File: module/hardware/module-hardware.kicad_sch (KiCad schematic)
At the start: 48 parts

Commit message: Start work on dsub pinout/connections
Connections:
- net +5V: now also J?.1 (Pin_1)
- net ASUM: now also J?.9 (Pin_9)
- net GND: now also J?.10 (Pin_10), J?.8 (Pin_8)
- net GPIO16_EXTRA: now reaches U?.27 (GPIO16)
- net GPIO17_DRDY: now reaches U?.28 (GPIO17)
- net GPIO18_SCK: now reaches U?.29 (GPIO18)
- net GPIO19_SDIN: now reaches U?.30 (GPIO19)
- net GPIO20_SDOUT: now reaches U?.31 (GPIO20)
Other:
- moved on the sheet: J?
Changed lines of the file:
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@@
   (junction (at 88.9 54.61) (diameter 0) (color 0 0 0 0)
+  )
+  (junction (at 76.2 191.77) (diameter 0) (color 0 0 0 0)
   )
   (junction (at 303.53 85.09) (diameter 0) (color 0 0 0 0)
@@
     (stroke (width 0) (type default) (color 0 0 0 0))
   )
-  (wire (pts (xy 240.03 237.49) (xy 243.84 237.49))
+  (wire (pts (xy 58.42 181.61) (xy 60.96 181.61))
+    (stroke (width 0) (type default) (color 0 0 0 0))
+  )
+  (wire (pts (xy 240.03 237.49) (xy 257.81 237.49))
     (stroke (width 0) (type default) (color 0 0 0 0))
   )
@@
     (stroke (width 0) (type default) (color 0 0 0 0))
   )
+  (wire (pts (xy 76.2 189.23) (xy 76.2 191.77))
+    (stroke (width 0) (type default) (color 0 0 0 0))
+  )
   (wire (pts (xy 180.34 123.19) (xy 180.34 130.81))
     (stroke (width 0) (type default) (color 0 0 0 0))
@@
     (stroke (width 0) (type default) (color 0 0 0 0))
   )
+  (wire (pts (xy 241.3 97.79) (xy 261.62 97.79))
+    (stroke (width 0) (type default) (color 0 0 0 0))
+  )
   (wire (pts (xy 179.07 34.29) (xy 179.07 30.48))
     (stroke (width 0) (type default) (color 0 0 0 0))
@@
     (stroke (width 0) (type default) (color 0 0 0 0))
   )
+  (wire (pts (xy 73.66 191.77) (xy 76.2 191.77))
+    (stroke (width 0) (type default) (color 0 0 0 0))
+  )
   (wire (pts (xy 57.15 54.61) (xy 63.5 54.61))
     (stroke (width 0) (type default) (color 0 0 0 0))
@@
     (stroke (width 0) (type default) (color 0 0 0 0))
   )
+  (wire (pts (xy 73.66 189.23) (xy 76.2 189.23))
+    (stroke (width 0) (type default) (color 0 0 0 0))
+  )
   (wire (pts (xy 60.96 240.03) (xy 71.12 240.03))
     (stroke (width 0) (type default) (color 0 0 0 0))
@@
     (stroke (width 0) (type default) (color 0 0 0 0))
   )
+  (wire (pts (xy 76.2 194.31) (xy 76.2 191.77))
+    (stroke (width 0) (type default) (color 0 0 0 0))
+  )
   (wire (pts (xy 289.56 30.48) (xy 289.56 34.29))
     (stroke (width 0) (type default) (color 0 0 0 0))
@@
     (stroke (width 0) (type default) (color 0 0 0 0))
   )
+  (wire (pts (xy 241.3 102.87) (xy 261.62 102.87))
+    (stroke (width 0) (type default) (color 0 0 0 0))
+  )
   (wire (pts (xy 201.93 30.48) (xy 201.93 34.29))
     (stroke (width 0) (type default) (color 0 0 0 0))
@@
     (stroke (width 0) (type default) (color 0 0 0 0))
   )
+  (wire (pts (xy 241.3 107.95) (xy 261.62 107.95))
+    (stroke (width 0) (type default) (color 0 0 0 0))
+  )
   (wire (pts (xy 80.01 130.81) (xy 74.93 130.81))
     (stroke (width 0) (type default) (color 0 0 0 0))
@@
     (stroke (width 0) (type default) (color 0 0 0 0))
   )
+  (wire (pts (xy 58.42 179.07) (xy 58.42 181.61))
+    (stroke (width 0) (type default) (color 0 0 0 0))
+  )
   (wire (pts (xy 339.09 101.6) (xy 351.79 101.6))
     (stroke (width 0) (type default) (color 0 0 0 0))
@@
     (stroke (width 0) (type default) (color 0 0 0 0))
   )
+  (wire (pts (xy 241.3 100.33) (xy 261.62 100.33))
+    (stroke (width 0) (type default) (color 0 0 0 0))
+  )
   (wire (pts (xy 162.56 111.76) (xy 162.56 113.03))
     (stroke (width 0) (type default) (color 0 0 0 0))
   )
+  (wire (pts (xy 52.07 191.77) (xy 60.96 191.77))
+    (stroke (width 0) (type default) (color 0 0 0 0))
+  )
   (wire (pts (xy 255.27 41.91) (xy 255.27 44.45))
     (stroke (width 0) (type default) (color 0 0 0 0))
@@
   )
   (wire (pts (xy 314.96 85.09) (xy 303.53 85.09))
+    (stroke (width 0) (type default) (color 0 0 0 0))
+  )
+  (wire (pts (xy 241.3 105.41) (xy 261.62 105.41))
     (stroke (width 0) (type default) (color 0 0 0 0))
   )
@@
     (effects (font (size 1.27 1.27)) (justify right bottom))
   )
+  (label "GPIO18_SCK" (at 261.62 102.87 180)
+    (effects (font (size 1.27 1.27)) (justify right bottom))
+  )
   (label "GPIO28_ADC2" (at 336.55 104.14 0)
     (effects (font (size 1.27 1.27)) (justify left bottom))
   )
+  (label "ASUM" (at 52.07 191.77 0)
+    (effects (font (size 1.27 1.27)) (justify left bottom))
+  )
   (label "GPIO26_ADC0" (at 336.55 80.01 0)
     (effects (font (size 1.27 1.27)) (justify left bottom))
+  )
+  (label "GPIO17_DRDY" (at 261.62 100.33 180)
+    (effects (font (size 1.27 1.27)) (justify right bottom))
+  )
+  (label "ASUM" (at 257.81 237.49 180)
+    (effects (font (size 1.27 1.27)) (justify right bottom))
   )
   (label "GPIO29_ADC3" (at 367.03 104.14 0)
@@
     (effects (font (size 1.27 1.27)) (justify right bottom))
   )
+  (label "GPIO20_SDOUT" (at 261.62 107.95 180)
+    (effects (font (size 1.27 1.27)) (justify right bottom))
+  )
+  (label "GPIO16_EXTRA" (at 261.62 97.79 180)
+    (effects (font (size 1.27 1.27)) (justify right bottom))
+  )
   (label "GPIO10_DAC_SCK" (at 261.62 82.55 180)
     (effects (font (size 1.27 1.27)) (justify right bottom))
@@
     (effects (font (size 1.27 1.27)) (justify right bottom))
   )
+  (label "GPIO19_SDIN" (at 261.62 105.41 180)
+    (effects (font (size 1.27 1.27)) (justify right bottom))
+  )
   (label "GPIO11_DAC_SDAT" (at 151.13 227.33 0)
     (effects (font (size 1.27 1.27)) (justify left bottom))
@@
   (label "GPIO9_DAC_CSB" (at 151.13 234.95 0)
     (effects (font (size 1.27 1.27)) (justify left bottom))
-  )
-  (global_label "ASUM" (shape output) (at 243.84 237.49 0) (fields_autoplaced)
-    (effects (font (size 1.27 1.27)) (justify left))
-    (property "Intersheet References" "${INTERSHEET_REFS}" (id 0) (at 251.3331 237.4106 0)
-      (effects (font (size 1.27 1.27)) (justify left) hide)
-    )
   )
   (symbol (lib_id "power:PWR_FLAG") (at 92.71 38.1 0) (unit 1)
@@
     (pin "1")
   )
+  (symbol (lib_id "power:+5V") (at 58.42 179.07 0) (unit 1)
+    (in_bom yes) (on_board yes) (fields_autoplaced)
+    (property "Reference" "#PWR?" (id 0) (at 58.42 182.88 0)
+      (effects (font (size 1.27 1.27)) hide)
+    )
+    (property "Value" "+5V" (id 1) (at 58.42 173.99 0))
+    (property "Footprint" "" (id 2) (at 58.42 179.07 0)
+      (effects (font (size 1.27 1.27)) hide)
+    )
+    (property "Datasheet" "" (id 3) (at 58.42 179.07 0)
+      (effects (font (size 1.27 1.27)) hide)
+    )
+    (pin "1")
+  )
   (symbol (lib_id "Device:R") (at 173.99 62.23 90) (unit 1)
     (in_bom yes) (on_board yes)
@@
     (pin "2")
   )
-  (symbol (lib_id "Connector_Generic:Conn_02x05_Odd_Even") (at 66.04 193.04 0) (unit 1)
-    (in_bom yes) (on_board yes) (fields_autoplaced)
-    (property "Reference" "J?" (id 0) (at 67.31 180.975 0))
-    (property "Value" "Conn_02x05_Odd_Even" (id 1) (at 67.31 183.515 0))
-    (property "Footprint" "" (id 2) (at 66.04 193.04 0)
-      (effects (font (size 1.27 1.27)) hide)
-    )
-    (property "Datasheet" "~" (id 3) (at 66.04 193.04 0)
+  (symbol (lib_id "Connector_Generic:Conn_02x05_Odd_Even") (at 66.04 186.69 0) (unit 1)
+    (in_bom yes) (on_board yes)
+    (property "Reference" "J?" (id 0) (at 67.31 174.625 0))
+    (property "Value" "Conn_02x05_Odd_Even" (id 1) (at 72.39 177.8 0))
+    (property "Footprint" "" (id 2) (at 66.04 186.69 0)
+      (effects (font (size 1.27 1.27)) hide)
+    )
+    (property "Datasheet" "~" (id 3) (at 66.04 186.69 0)
       (effects (font (size 1.27 1.27)) hide)
     )
@@
     (pin "1")
   )
-  (symbol (lib_id "Connector_Generic:Conn_02x05_Odd_Even") (at 103.505 192.405 0) (unit 1)
-    (in_bom yes) (on_board yes) (fields_autoplaced)
-    (property "Reference" "J?" (id 0) (at 104.775 180.34 0))
-    (property "Value" "Conn_02x05_Odd_Even" (id 1) (at 104.775 182.88 0))
-    (property "Footprint" "" (id 2) (at 103.505 192.405 0)
-      (effects (font (size 1.27 1.27)) hide)
-    )
-    (property "Datasheet" "~" (id 3) (at 103.505 192.405 0)
+  (symbol (lib_id "Connector_Generic:Conn_02x05_Odd_Even") (at 109.22 186.69 0) (unit 1)
+    (in_bom yes) (on_board yes) (fields_autoplaced)
+    (property "Reference" "J?" (id 0) (at 110.49 174.625 0))
+    (property "Value" "Conn_02x05_Odd_Even" (id 1) (at 110.49 177.165 0))
+    (property "Footprint" "" (id 2) (at 109.22 186.69 0)
+      (effects (font (size 1.27 1.27)) hide)
+    )
+    (property "Datasheet" "~" (id 3) (at 109.22 186.69 0)
       (effects (font (size 1.27 1.27)) hide)
     )
@@
     )
     (property "Datasheet" "" (id 3) (at 187.96 143.51 0)
+      (effects (font (size 1.27 1.27)) hide)
+    )
+    (pin "1")
+  )
+  (symbol (lib_id "power:GND") (at 76.2 194.31 0) (unit 1)
+    (in_bom yes) (on_board yes) (fields_autoplaced)
+    (property "Reference" "#PWR?" (id 0) (at 76.2 200.66 0)
+      (effects (font (size 1.27 1.27)) hide)
+    )
+    (property "Value" "GND" (id 1) (at 76.2 199.39 0))
+    (property "Footprint" "" (id 2) (at 76.2 194.31 0)
+      (effects (font (size 1.27 1.27)) hide)
+    )
+    (property "Datasheet" "" (id 3) (at 76.2 194.31 0)
       (effects (font (size 1.27 1.27)) hide)
     )
@@
       (reference "#PWR?") (unit 1) (value "GND") (footprint "")
     )
+    (path "/1eced8f1-fcc8-4121-ae1f-727d47435957"
+      (reference "#PWR?") (unit 1) (value "+5V") (footprint "")
+    )
     (path "/24f789e3-a318-4855-a56f-29afa0155580"
       (reference "#PWR?") (unit 1) (value "+3V3") (footprint "")
@@
       (reference "#PWR?") (unit 1) (value "GND") (footprint "")
     )
+    (path "/b2a71297-139f-414d-9936-936167d27c2a"
+      (reference "#PWR?") (unit 1) (value "GND") (footprint "")
+    )

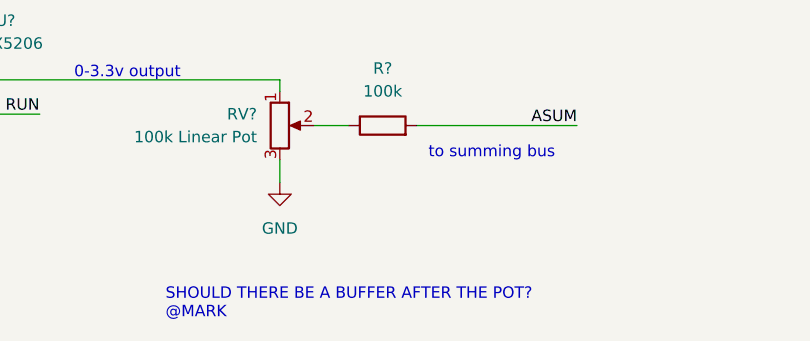
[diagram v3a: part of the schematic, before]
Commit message: Add module schematic TODO
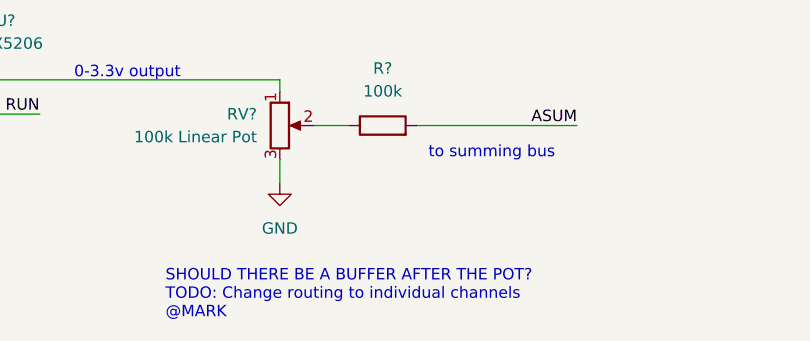
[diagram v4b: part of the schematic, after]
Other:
- note added: "SHOULD THERE BE A BUFFER AFTER THE POT? TODO: Change routing to individual channels @MARK"
- note removed: "SHOULD THERE BE A BUFFER AFTER THE POT? @MARK"
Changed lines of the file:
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@@
     (effects (font (size 2.54 2.54) (thickness 0.508) bold italic) (justify left bottom))
   )
-  (text "SHOULD THERE BE A BUFFER AFTER THE POT?\n@MARK" (at 212.09 259.08 0)
+  (text "SHOULD THERE BE A BUFFER AFTER THE POT?\nTODO: Change routing to individual channels\n@MARK"
+    (at 212.09 259.08 0)
     (effects (font (size 1.27 1.27)) (justify left bottom))
   )

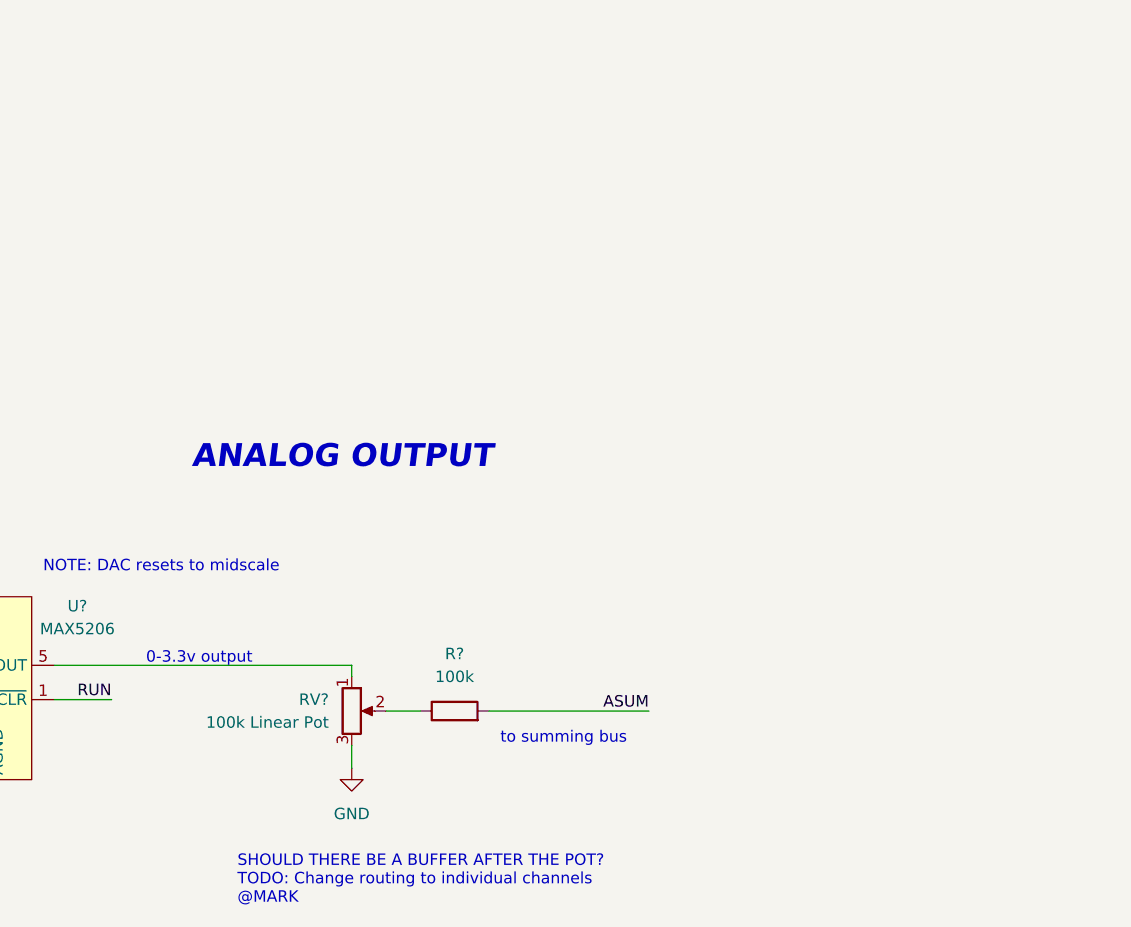
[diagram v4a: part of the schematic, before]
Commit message: Added analog mux to custom symbol library
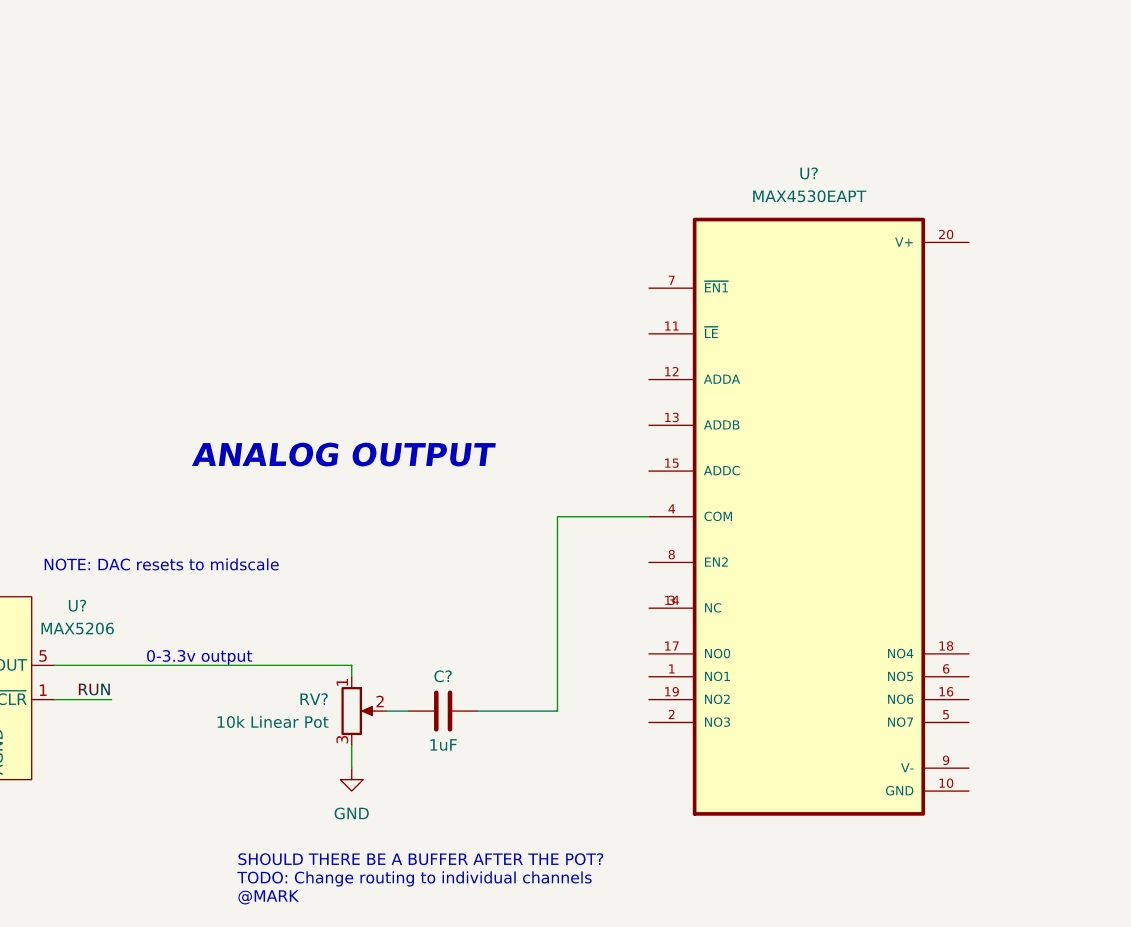
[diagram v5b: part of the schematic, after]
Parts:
- removed R?: 100k, symbol Device:R
- added C?: 1uF, symbol Device:C
- added U?: MAX4530EAPT, SOP65P777X199-20N, symbol DRUM_Custom:MAX4530EAPT
- RV?: value 100k Linear Pot -> 10k Linear Pot
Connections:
- net at RV?.2: now also C?.1
- new net: U?.14 (NC), U?.3 (NC)
- new net: C?.2, U?.4 (COM)
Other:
- note removed: "to summing bus"
